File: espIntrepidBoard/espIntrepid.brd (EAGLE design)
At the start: 56 x 56 mm, 24 parts, among them Q1 TRANS_NPN, Q2 TRANS_NPN, Q3 TRANS_NPN, Q4 TRANS_PNP, Q5 TRANS_PNP, Q6 TRANS_PNP, Q7 TRANS_NPN, U1 ESP32DEV_38, U2 MOSFET_P, U3 MOSFET_P, U4 MOSFET_P

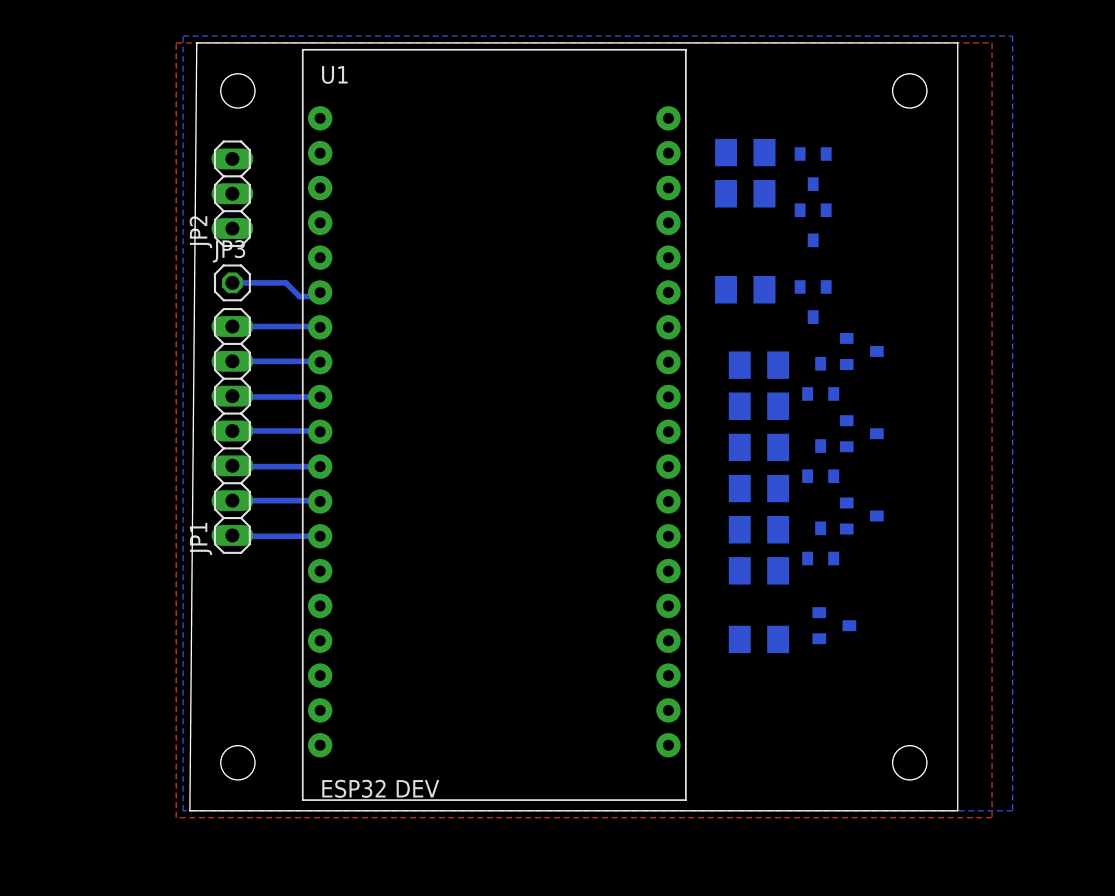
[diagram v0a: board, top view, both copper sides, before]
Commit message: Started board routing
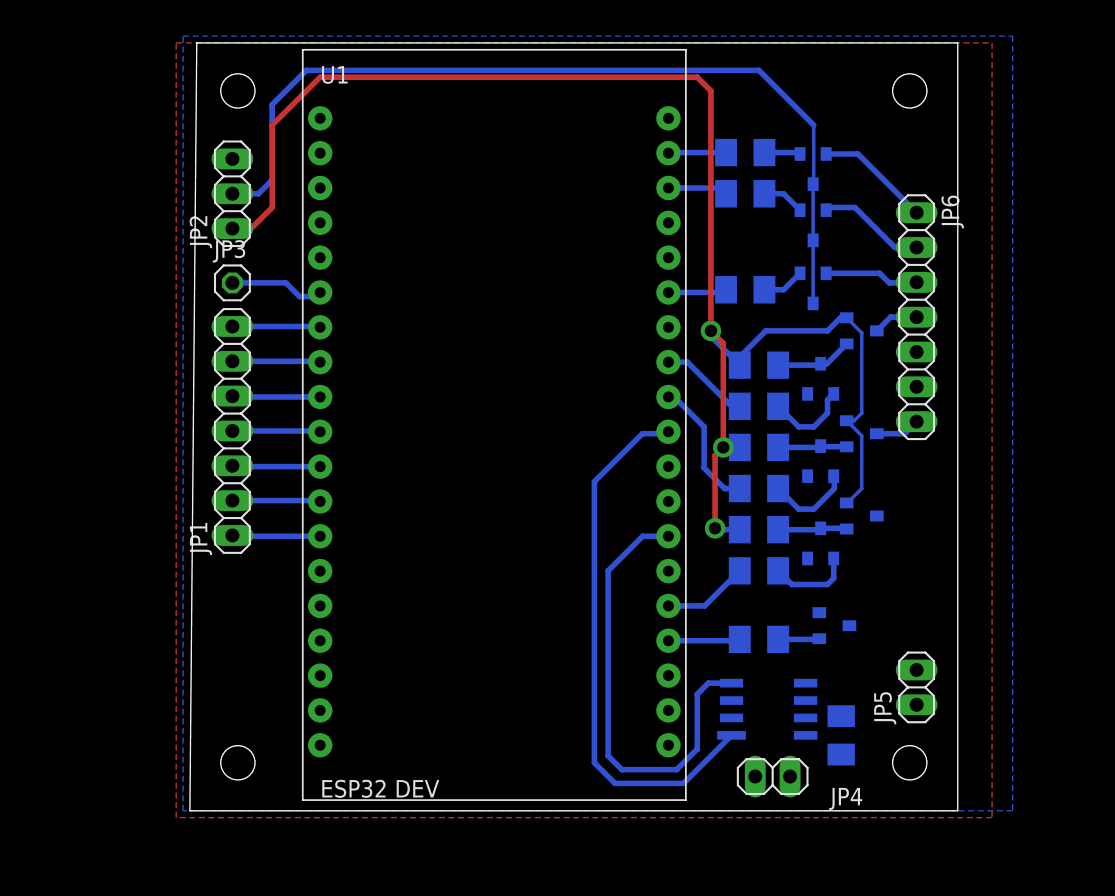
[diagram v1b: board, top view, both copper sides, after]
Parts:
- added JP4, JP5: (no value), pinhead:1X02
- added JP6: (no value), pinhead:1X07
- added R11: (no value), DR:M1206
- added U5: SN65HVD232DSOIC8, DR:SOIC-8
- moved U2 1.50 mm to (50.0, 35.0)
- moved Q6 1.00 mm to (45.5, 37.1)
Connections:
- new net CAN_RX: U1.26, U5.4
- new net CAN_TX: U1.29, U5.1
- new net N$19: JP4.2, JP5.2, U5.6
- new net N$21: JP4.1, R11.2
- new net N$3: JP5.1, R11.1, U5.7
- net ABS: now also JP6.2
- net AIRBAG: now also JP6.1
- net BACKLIGHTS: now also JP6.5
- net BL_UC: now also U1.23; no longer U1.24
- net GND: now also U5.2
- net HBEAM: now also JP6.6
- net LTURN: now also JP6.7
- net LTURN_UC: now also U1.24; no longer U1.23
- net OIL: now also JP6.3
- net RTURN: now also JP6.4
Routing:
- net +12V: track 0.00 -> 106.4 mm, vias 0 -> 3
- net +5V: track 0.00 -> 64.0 mm
- net CAN_TX: track 0.00 -> 39.5 mm
- net CAN_RX: track 0.00 -> 33.3 mm
- net RTURN_UC: track 0.00 -> 9.72 mm
- net AIRBAG: track 0.00 -> 8.37 mm
- net ABS: track 0.00 -> 7.89 mm
- net OIL: track 0.00 -> 6.91 mm
- net HB_UC: track 0.00 -> 6.53 mm
- net N$11: track 0.00 -> 6.26 mm
- net LTURN_UC: track 0.00 -> 6.26 mm
- net N$12: track 0.00 -> 6.22 mm
- net N$17: track 0.00 -> 6.10 mm
- net N$13: track 0.00 -> 5.64 mm
- net BL_UC: track 0.00 -> 5.24 mm
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
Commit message: Using optoisolators
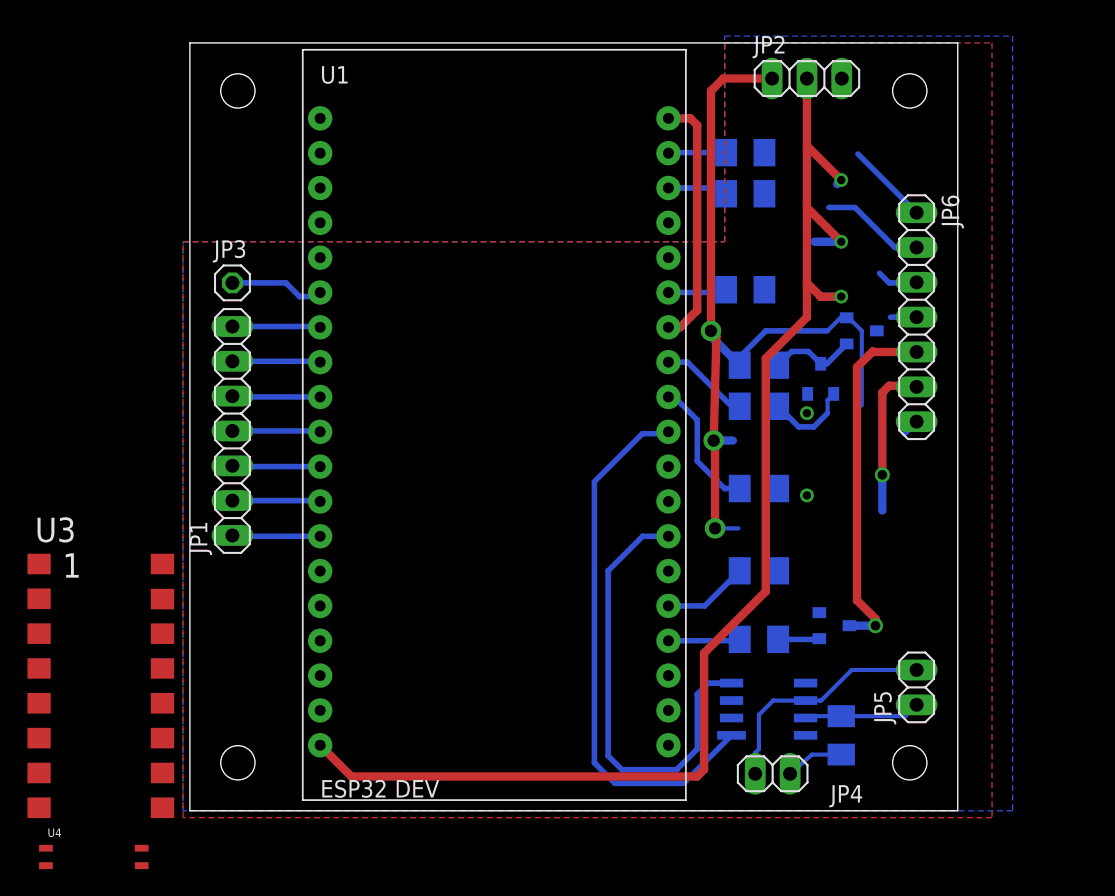
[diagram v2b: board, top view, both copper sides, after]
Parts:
- removed Q2, Q3: TRANS_NPN, DR:SOT-23
- removed Q4, Q5, Q6: TRANS_PNP, DR:SOT-23
- removed R2, R3: (no value), DR:M1206
- U3: value MOSFET_P -> LTV-847; device DR:SOT-23 -> DR:SM-16
- U4: value MOSFET_P -> PS2801C-1; device DR:SOT-23 -> SureFireParts 6.0:4-SSOP
- moved U4 65.7 mm to (-10.5, -4.00), flipped to the top, turned to 0 degrees
- moved U3 61.7 mm to (-11.0, 18.0), flipped to the top, turned to 0 degrees
- moved JP2 42.7 mm to (45.0, 53.4), turned to 0 degrees
- moved JP4 0.20 mm to (42.5, 2.70)
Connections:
- removed net N$16: Q3.3, R3.1, U4.1
- removed net N$22: Q4.1, R7.2
- removed net N$23: Q5.1, R8.2
- removed net N$24: Q6.1, R9.2
- new net N$15: R7.2, U3.5
- new net N$2: R5.2, U3.1
- net +12V: now also U3.14, U3.16; no longer R2.2, R3.2, U3.2, U4.2
- net +5V: now also U3.10, U3.12, U4.4; no longer Q4.3, Q5.3, Q6.3
- net ABS: now also U3.9; no longer Q5.2
- net AIRBAG: now also U3.11; no longer Q4.2
- net GND: now also U3.2, U3.4, U3.6, U3.8, U4.2; no longer Q2.2, Q3.2
- net HBEAM: now also U2.3; no longer U4.3
- net LTURN: now also U3.13; no longer U3.3
- net N$11: now also R8.2, U3.7; no longer Q2.1, R5.2
- net N$14: now also R6.2, U3.3; no longer Q2.3, R2.1, U3.1
- net N$17: now also R9.2, U4.1; no longer Q3.1, R6.2
- net OIL: now also U4.3; no longer Q6.2
- net RTURN: now also U3.15; no longer U2.3
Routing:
- net +12V: track 106.4 -> 60.1 mm
- net +5V: track 64.0 -> 96.6 mm, vias 0 -> 3
- net BACKLIGHTS: track 0.00 -> 26.2 mm, vias 0 -> 1
- net GND: track 0.00 -> 18.4 mm, vias 0 -> 2
- net N$19: track 0.00 -> 17.3 mm
- net HBEAM: track 0.00 -> 11.3 mm, vias 0 -> 1
- net N$3: track 0.00 -> 8.50 mm
- net N$11: track 6.26 -> 0.00 mm
- net N$17: track 6.10 -> 0.00 mm
- net N$14: track 5.09 -> 0.00 mm
- net N$16: track 5.06 -> 0.00 mm
- net N$21: track 0.00 -> 4.26 mm
- net OIL: track 6.91 -> 3.01 mm
- net N$24: track 3.10 -> 0.00 mm
- net N$23: track 3.10 -> 0.00 mm
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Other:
- outline, holes or cut-outs redrawn

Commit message: Created esp32 arduino program
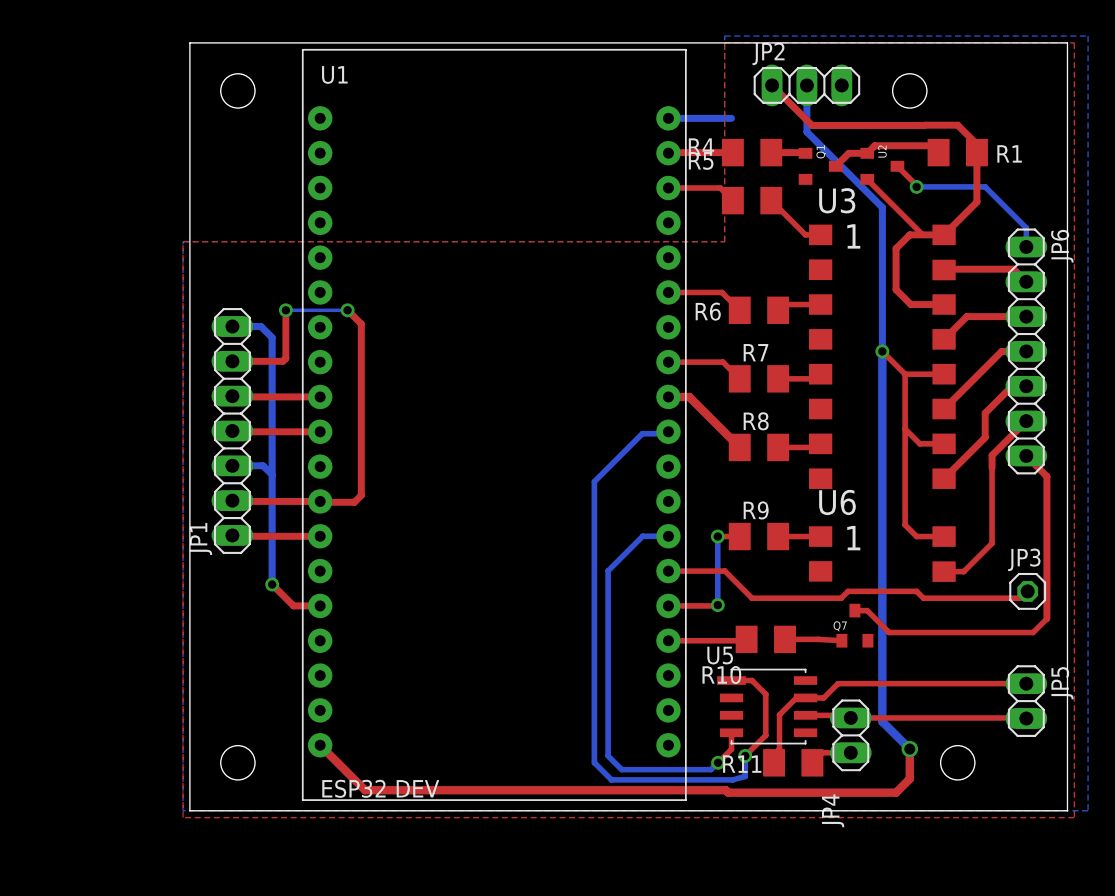
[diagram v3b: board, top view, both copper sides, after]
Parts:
- removed U4: PS2801C-1, SureFireParts 6.0:4-SSOP
- added U6: LTV-817, DR:SM-4
- moved JP3 62.2 mm to (61.1, 16.0)
- moved U3 61.8 mm to (46.0, 42.0)
- moved R1 21.2 mm to (56.0, 48.0), flipped to the top
- moved R5 21.0 mm to (41.0, 44.5), flipped to the top, turned to 0 degrees
- moved R6 19.0 mm to (41.5, 36.5), flipped to the top, turned to 0 degrees
- moved R8 18.5 mm to (41.5, 26.5), flipped to the top, turned to 0 degrees
- moved R4 18.5 mm to (41.0, 48.0), flipped to the top, turned to 0 degrees
- moved R9 18.0 mm to (41.5, 20.0), flipped to the top, turned to 0 degrees
- moved R7 16.5 mm to (41.5, 31.5), flipped to the top, turned to 0 degrees
- moved Q1 14.5 mm to (47.0, 47.0), flipped to the top, turned to 270 degrees
- moved U2 12.1 mm to (51.5, 47.0), flipped to the top, turned to 270 degrees
- moved JP6 8.38 mm to (61.0, 33.5)
- moved JP5 8.06 mm to (61.0, 8.00), turned to 270 degrees
- moved JP4 6.35 mm to (48.2, 5.50), turned to 90 degrees
- moved R11 4.03 mm to (44.0, 3.50), flipped to the top, turned to 0 degrees
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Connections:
- removed net N$4 (its old number): JP1.7, U1.7
- removed net N$5 (its old number): JP1.6, U1.8
- removed net N$9: JP1.2, U1.12
- removed net PB: JP3.1, U1.6
- new net N$16: R9.2, U6.1
- new net N$7: JP1.3, JP1.7, U1.15
- net +5V: now also U6.4; no longer U4.4
- net ABS: now also JP6.5; no longer JP6.2
- net ABS_UC: now also U1.30; no longer U1.36
- net AIRBAG: now also JP6.4; no longer JP6.1
- net AIRBAG_UC: now also U1.31; no longer U1.37
- net BACKLIGHTS: now also JP6.7; no longer JP6.5
- net GND: now also U6.2; no longer U4.2
- net HBEAM: now also JP6.1; no longer JP6.6
- net HB_UC: now also U1.37; no longer U1.31
- net LTURN: now also JP6.3; no longer JP6.7
- net LTURN_UC: now also U1.33; no longer U1.24
- net N$17: now also JP3.1, U1.25; no longer R9.2, U4.1
- net N$8: now also JP1.2, JP1.6, U1.12; no longer JP1.3, U1.11
- net OIL: now also JP6.6, U6.3; no longer JP6.3, U4.3
- net OIL_UC: now also U1.24; no longer U1.33
- net RTURN: now also JP6.2; no longer JP6.4
- net RTURN_UC: now also U1.36; no longer U1.30
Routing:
- net N$8: track 6.42 -> 35.6 mm, vias 0 -> 2
- net N$7: track 0.00 -> 28.6 mm, vias 0 -> 1
- net N$17: track 0.00 -> 27.6 mm
- net +5V: track 96.6 -> 121.2 mm, vias 3 -> 2
- net +12V: track 60.1 -> 42.5 mm, vias 3 -> 0
- net N$3: track 8.50 -> 22.6 mm
- net GND: track 18.4 -> 4.60 mm, vias 2 -> 0
- net OIL: track 3.01 -> 14.3 mm
- net CAN_TX: track 39.5 -> 48.5 mm, vias 0 -> 1
- net PB: track 6.94 -> 0.00 mm
- net N$9: track 6.42 -> 0.00 mm
- net N$5 (its old number): track 6.42 -> 0.00 mm
- net N$4 (its old number): track 6.42 -> 0.00 mm
- net OIL_UC: track 4.28 -> 10.2 mm, vias 0 -> 2
- net LTURN: track 1.24 -> 6.69 mm
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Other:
- board size 56 x 56 mm -> 64 x 56 mm

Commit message: Made improvements to board (small stuff)
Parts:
- added JP7: (no value), pinhead:1X02
- moved JP5 0.38 mm to (61.0, 8.38)
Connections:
- net +12V: now also JP7.1
- net GND: now also JP7.2
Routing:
- net +12V: track 42.5 -> 79.1 mm, vias 0 -> 1
- net +5V: track 121.2 -> 119.1 mm
